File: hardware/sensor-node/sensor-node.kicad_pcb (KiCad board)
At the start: 2 copper layers, 57 x 57 mm, 52 parts, among them J1 CONUFL001-SMD-T, J2 Conn_ARM_JTAG_SWD_10, Q1 PMV250EPEA, U1 TLV61225, U2 TPS27081A, U3 SHT31-DIS, U4 24LC32, U5 MLX90614, U6 ADG633YRU, U7 TSV911RILT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

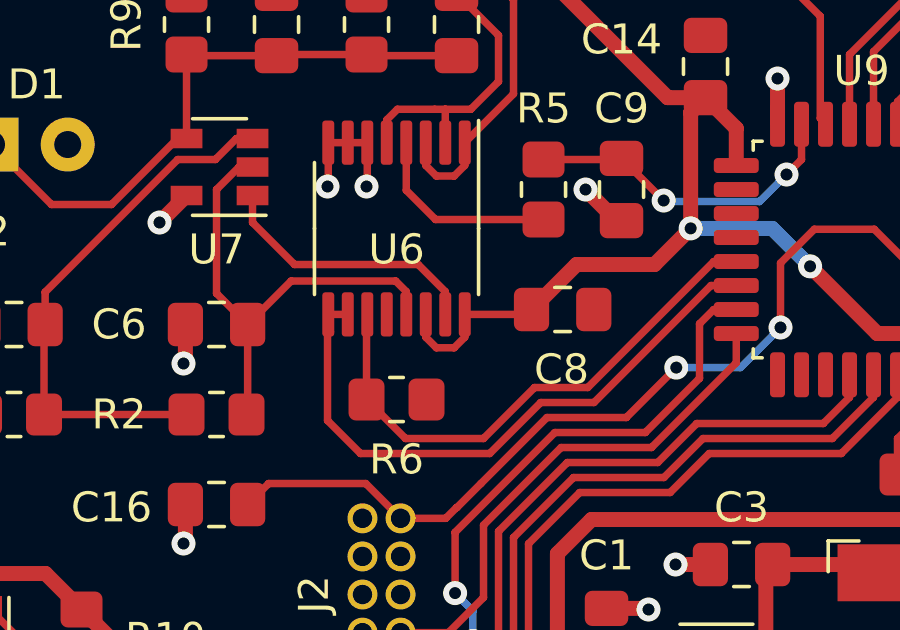
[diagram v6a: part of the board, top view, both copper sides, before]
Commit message: Update C9 pad 2
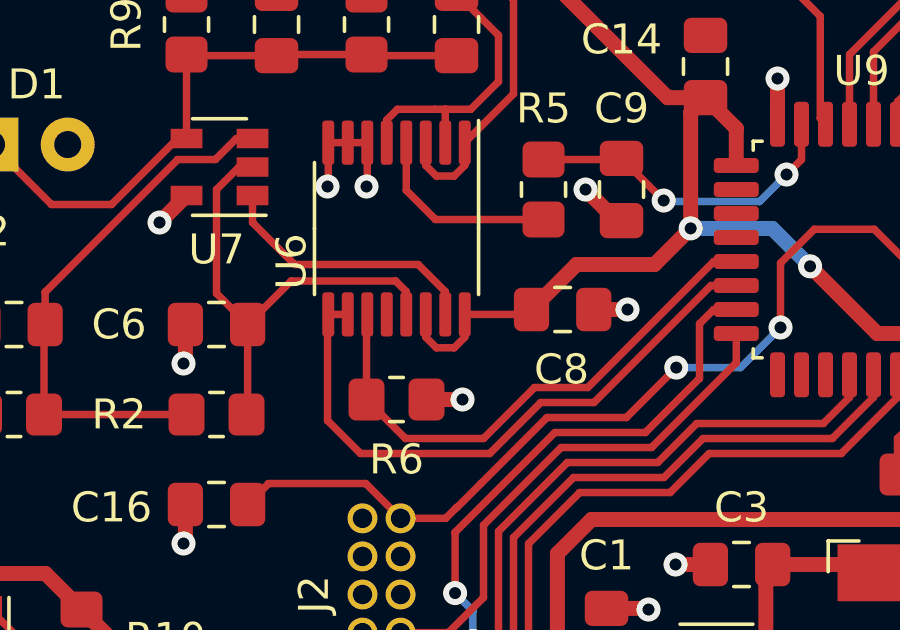
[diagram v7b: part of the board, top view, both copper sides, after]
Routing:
- net GND: track 56.3 -> 58.6 mm, vias 106 -> 108
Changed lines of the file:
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@@
     (thickness 1.6002)
     (drawings 27)
-    (tracks 531)
+    (tracks 535)
     (zones 0)
     (modules 52)
@@
   )
   (setup
-    (last_trace_width 0.25)
+    (last_trace_width 0.5)
     (user_trace_width 0.1)
     (user_trace_width 0.2)
@@
     (tags "TSSOP SO")
     (attr smd)
-    (fp_text reference U6 (at 0.7 0 180) (layer F.SilkS)
+    (fp_text reference U6 (at 1.1 3.5 270) (layer F.SilkS)
       (effects (font (size 1 1) (thickness 0.15)))
     )
@@
   (segment (start 127.525 72.875) (end 127.5 72.9) (width 0.25) (layer Front) (net 1))
   (segment (start 127.525 71.4375) (end 127.525 72.875) (width 0.25) (layer Front) (net 1))
+  (via (at 130.7 80) (size 0.8) (drill 0.4) (layers Front Back) (net 1))
+  (segment (start 129.5 80) (end 130.7 80) (width 0.5) (layer Front) (net 1))
+  (via (at 136.2 77) (size 0.8) (drill 0.4) (layers Front Back) (net 1))
+  (segment (start 135.075 77) (end 136.2 77) (width 0.5) (layer Front) (net 1))
   (segment (start 150.5 91.31) (end 151.45 91.31) (width 0.5) (layer Front) (net 2))
   (segment (start 150.5 95.5) (end 150.5 91.31) (width 0.5) (layer Front) (net 2))

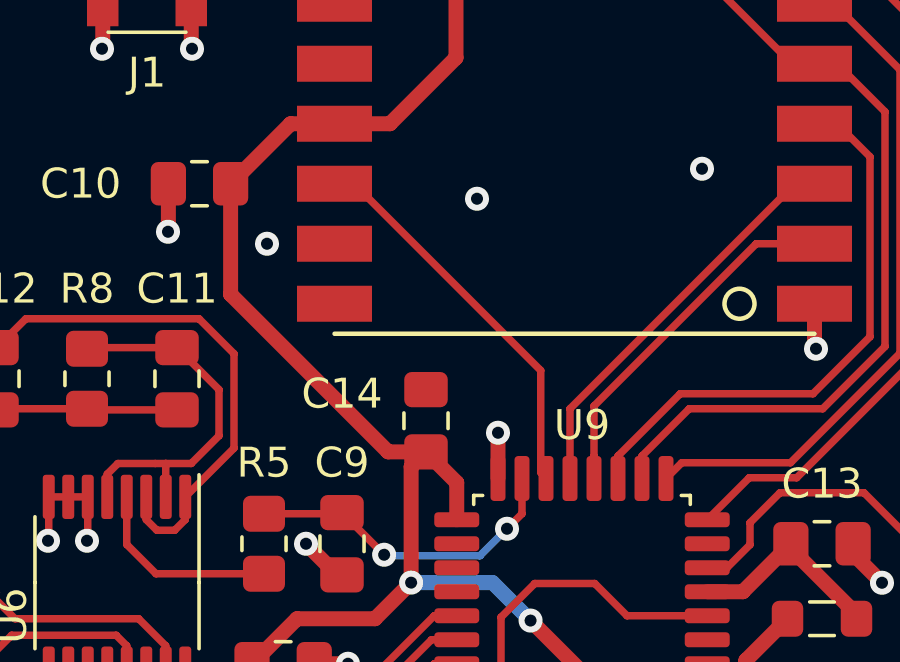
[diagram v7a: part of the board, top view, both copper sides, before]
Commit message: Perform parts pinout check
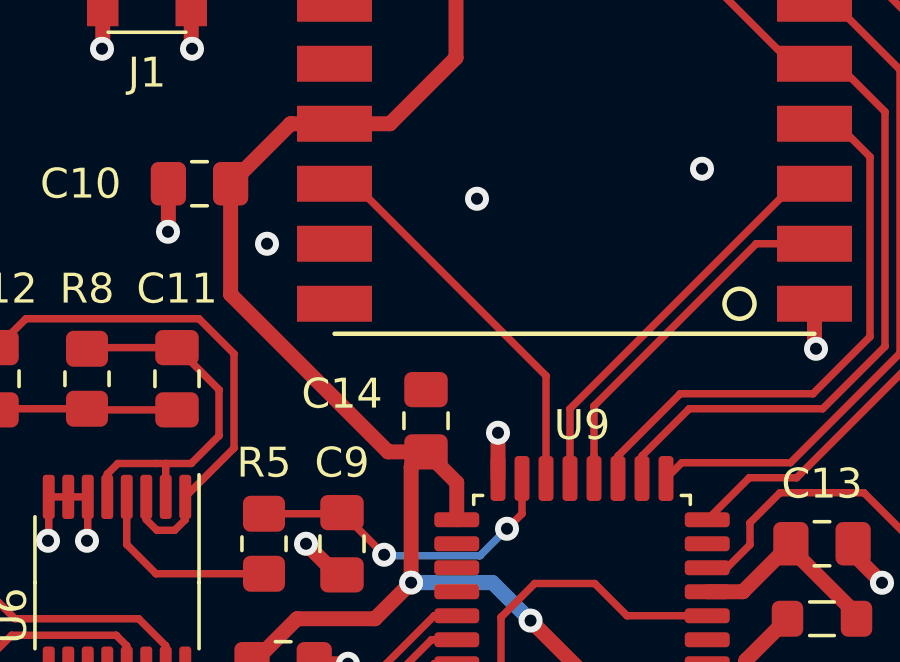
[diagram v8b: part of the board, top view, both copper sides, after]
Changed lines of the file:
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@@
     (thickness 1.6002)
     (drawings 27)
-    (tracks 535)
+    (tracks 533)
     (zones 0)
     (modules 52)
@@
   (segment (start 135.75 59) (end 134.2875 59) (width 0.5) (layer Front) (net 5))
   (segment (start 132.2875 61) (end 132.2875 64.6875) (width 0.5) (layer Front) (net 5))
+  (segment (start 137.5375 69.9375) (end 138.8 69.9375) (width 0.5) (layer Front) (net 5))
+  (segment (start 132.2875 64.6875) (end 137.5375 69.9375) (width 0.5) (layer Front) (net 5))
   (segment (start 127.365 89.747106) (end 127.365 89.04) (width 0.5) (layer Back) (net 5))
   (via (at 128 91.97502) (size 0.8) (drill 0.4) (layers Front Back) (net 5))
@@
   (segment (start 132.8375 77.1625) (end 133 77) (width 0.25) (layer Front) (net 5))
   (segment (start 130.775 77.1625) (end 132.8375 77.1625) (width 0.25) (layer Front) (net 5))
-  (segment (start 137.5375 69.9375) (end 138.8 69.9375) (width 0.5) (layer Front) (net 5))
-  (segment (start 132.2875 64.6875) (end 137.5375 69.9375) (width 0.5) (layer Front) (net 5))
   (segment (start 133 77) (end 134.5 75.5) (width 0.5) (layer Front) (net 5))
   (segment (start 134.5 75.5) (end 137.1 75.5) (width 0.5) (layer Front) (net 5))
+  (segment (start 137.1 75.5) (end 138.304512 74.295488) (width 0.5) (layer Front) (net 5))
   (segment (start 138.304512 70.432988) (end 138.8 69.9375) (width 0.5) (layer Front) (net 5))
   (segment (start 138.304512 74.295488) (end 138.304512 70.432988) (width 0.5) (layer Front) (net 5))
-  (segment (start 137.1 75.5) (end 138.304512 74.295488) (width 0.5) (layer Front) (net 5))
   (segment (start 139.825 70.9625) (end 138.8 69.9375) (width 0.5) (layer Front) (net 5))
   (segment (start 139.825 72.2) (end 139.825 70.9625) (width 0.5) (layer Front) (net 5))
@@
   (segment (start 148.175 77.8) (end 144.52499 77.8) (width 0.5) (layer Front) (net 5))
   (segment (start 149.4625 82.7375) (end 149.4625 80) (width 0.5) (layer Front) (net 5))
-  (segment (start 148.2 84) (end 149.4625 82.7375) (width 0.5) (layer Front) (net 5))
-  (segment (start 135 84) (end 148.2 84) (width 0.5) (layer Front) (net 5))
-  (segment (start 133.8625 85.1375) (end 135 84) (width 0.5) (layer Front) (net 5))
   (segment (start 133.8625 89.0375) (end 133.8625 85.1375) (width 0.5) (layer Front) (net 5))
+  (segment (start 133.8625 85.1375) (end 135 84) (width 0.5) (layer Front) (net 5))
+  (segment (start 135 84) (end 148.2 84) (width 0.5) (layer Front) (net 5))
+  (segment (start 148.2 84) (end 149.4625 82.7375) (width 0.5) (layer Front) (net 5))
   (via (at 137.82499 78.93592) (size 0.8) (drill 0.4) (layers Front Back) (net 6))
   (segment (start 133.514222 80.600022) (end 131.314244 82.8) (width 0.25) (layer Front) (net 6))
@@
   (segment (start 151.75 53) (end 152.5 53) (width 0.25) (layer Front) (net 28))
   (segment (start 136.4 61) (end 135.75 61) (width 0.25) (layer Front) (net 31))
-  (segment (start 142.62501 67.22501) (end 136.4 61) (width 0.25) (layer Front) (net 31))
-  (segment (start 142.62501 70.62501) (end 142.62501 67.22501) (width 0.25) (layer Front) (net 31))
-  (segment (start 142.8 70.8) (end 142.62501 70.62501) (width 0.25) (layer Front) (net 31))
-  (segment (start 142.8 70.825) (end 142.8 70.8) (width 0.25) (layer Front) (net 31))
+  (segment (start 142.8 67.4) (end 136.4 61) (width 0.25) (layer Front) (net 31))
+  (segment (start 142.8 70.825) (end 142.8 67.4) (width 0.25) (layer Front) (net 31))
   (segment (start 123.5375 80.4625) (end 123.5 80.5) (width 0.25) (layer Front) (net 39))
   (segment (start 123.5375 77.5) (end 123.5375 80.4625) (width 0.25) (layer Front) (net 39))
